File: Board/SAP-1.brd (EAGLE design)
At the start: 100 x 100 mm, 113 parts

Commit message: added RAM module and MAR
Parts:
- added MEMORY_ADDRESS_REGISTER:C1, MEMORY_ADDRESS_REGISTER:C2, RAM:C1, RAM:C10, RAM:C2, RAM:C3, RAM:C4, RAM:C5, RAM:C6, RAM:C7, RAM:C8, RAM:C9: 100n, rcl:C050-024X044
- added MEMORY_ADDRESS_REGISTER:IC1: 74LS173N, 74xx-us:DIL16
- added MEMORY_ADDRESS_REGISTER:IC2, RAM:IC6, RAM:IC7, RAM:IC8: 74LS157N, 74xx-us:DIL16
- added MEMORY_ADDRESS_REGISTER:LED1, MEMORY_ADDRESS_REGISTER:LED2, MEMORY_ADDRESS_REGISTER:LED3, MEMORY_ADDRESS_REGISTER:LED4, RAM:LED1, RAM:LED2, RAM:LED3, RAM:LED4: BLUE, led:LED3MM
- added MEMORY_ADDRESS_REGISTER:PROG: RED, led:LED3MM
- added MEMORY_ADDRESS_REGISTER:R1, MEMORY_ADDRESS_REGISTER:R10, MEMORY_ADDRESS_REGISTER:R2, MEMORY_ADDRESS_REGISTER:R3, MEMORY_ADDRESS_REGISTER:R4, MEMORY_ADDRESS_REGISTER:R9, RAM:R1, RAM:R2, RAM:R3, RAM:R4, RAM:R5, RAM:R6, RAM:R7, RAM:R8: 220, rcl:0204/7
- added MEMORY_ADDRESS_REGISTER:RUN: GREEN, led:LED3MM
- added MEMORY_ADDRESS_REGISTER:S1: Memory Address, switch-dil:DIP04YL
- added MEMORY_ADDRESS_REGISTER:S3: (no value), SparkFun-Switches:SWITCH_SPDT_PTH_11.6X4.0MM_KIT
- added RAM:IC1, RAM:IC2: 74LS189LSN, SAP-1:DIL16
- added RAM:IC3: 74LS245N, 74xx-us:DIL20
- added RAM:IC4, RAM:IC5: 74LS04N, 74xx-us:DIL14
- added RAM:IC9: 74ALS00N, 74xx-us:DIL14
- added RAM:LED5, RAM:LED6, RAM:LED7, RAM:LED8: YELLOW, led:LED3MM
- added RAM:R9: 1k, rcl:0204/7
- added RAM:S1: Write, SparkFun-Switches:TACTILE_SWITCH_PTH_12MM
- added RAM:S2: Memory Data, switch-dil:DIP08YL
- renumbered ALU1:IC1 to ALU:IC1, ALU1:IC2 to ALU:IC2, ALU1:IC3 to ALU:IC3, ALU1:IC4 to ALU:IC4, ALU1:IC5 to ALU:IC5, ALU1:LED1 to ALU:LED1, ALU1:LED2 to ALU:LED2, ALU1:LED3 to ALU:LED3, ALU1:LED4 to ALU:LED4, ALU1:LED5 to ALU:LED5, ALU1:LED6 to ALU:LED6, ALU1:LED7 to ALU:LED7, ALU1:LED8 to ALU:LED8, ALU1:R1 to ALU:R1, ALU1:R2 to ALU:R2, ALU1:R3 to ALU:R3, ALU1:R4 to ALU:R4, ALU1:R5 to ALU:R5, ALU1:R6 to ALU:R6, ALU1:R7 to ALU:R7, ALU1:R8 to ALU:R8
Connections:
- net ALU1:!ENABLE renamed !E0
- net ALU1:CARRY renamed CY
- net ALU1:GND renamed ALU:GND
- net ALU1:N$1 renamed ALU:N$1
- net ALU1:N$18 renamed ALU:N$18
- net ALU1:N$19 renamed ALU:N$19
- net ALU1:N$2 renamed ALU:N$2
- net ALU1:N$20 renamed ALU:N$20
- net ALU1:N$21 renamed ALU:N$21
- net ALU1:N$22 renamed ALU:N$22
- net ALU1:N$23 renamed ALU:N$23
- net ALU1:N$24 renamed ALU:N$24
- net ALU1:N$25 renamed ALU:N$25
- net ALU1:N$3 renamed ALU:N$3
- net ALU1:N$4 renamed ALU:N$4
- net ALU1:N$5 renamed ALU:N$5
- net ALU1:N$6 renamed ALU:N$6
- net ALU1:N$7 renamed ALU:N$7
- net ALU1:N$8 renamed ALU:N$8
- net ALU1:N$9 renamed ALU:N$9
- net ALU1:S1 renamed ALU:S1
- net ALU1:S2 renamed ALU:S2
- net ALU1:S3 renamed ALU:S3
- net ALU1:S4 renamed ALU:S4
- net ALU1:S5 renamed ALU:S5
- net ALU1:S6 renamed ALU:S6
- net ALU1:S7 renamed ALU:S7
- net ALU1:S8 renamed ALU:S8
- net ALU1:SU renamed SU
- net ALU1:VCC renamed ALU:VCC
- net CLK:CLK_HLT renamed HLT
- net IR:!ENABLE renamed !IO
- net IR:!LOAD renamed !II
- net RA:!ENABLE renamed !AO
- net RA:!LOAD renamed !AI
- net RB:!ENABLE renamed !BO
- net RB:!LOAD renamed !BI
- new net !MI: MEMORY_ADDRESS_REGISTER:IC1.10, MEMORY_ADDRESS_REGISTER:IC1.9
- new net !RO: RAM:IC3.19
- new net MEMORY_ADDRESS_REGISTER:CLK_IN: MEMORY_ADDRESS_REGISTER:IC1.7
- new net MEMORY_ADDRESS_REGISTER:CLR: MEMORY_ADDRESS_REGISTER:IC1.15
- new net MEMORY_ADDRESS_REGISTER:GND: MEMORY_ADDRESS_REGISTER:C1.2, MEMORY_ADDRESS_REGISTER:C2.2, MEMORY_ADDRESS_REGISTER:IC1.1, MEMORY_ADDRESS_REGISTER:IC1.2, MEMORY_ADDRESS_REGISTER:IC1.8, MEMORY_ADDRESS_REGISTER:IC2.15, MEMORY_ADDRESS_REGISTER:IC2.8, MEMORY_ADDRESS_REGISTER:R1.2, MEMORY_ADDRESS_REGISTER:R2.2, MEMORY_ADDRESS_REGISTER:R3.2, MEMORY_ADDRESS_REGISTER:R4.2, MEMORY_ADDRESS_REGISTER:S1.1, MEMORY_ADDRESS_REGISTER:S1.2, MEMORY_ADDRESS_REGISTER:S1.3, MEMORY_ADDRESS_REGISTER:S1.4, MEMORY_ADDRESS_REGISTER:S3.2
- new net MEMORY_ADDRESS_REGISTER:I5: MEMORY_ADDRESS_REGISTER:IC1.3, MEMORY_ADDRESS_REGISTER:IC2.3
- new net MEMORY_ADDRESS_REGISTER:I6: MEMORY_ADDRESS_REGISTER:IC1.4, MEMORY_ADDRESS_REGISTER:IC2.6
- new net MEMORY_ADDRESS_REGISTER:I7: MEMORY_ADDRESS_REGISTER:IC1.5, MEMORY_ADDRESS_REGISTER:IC2.10
- new net MEMORY_ADDRESS_REGISTER:I8: MEMORY_ADDRESS_REGISTER:IC1.6, MEMORY_ADDRESS_REGISTER:IC2.13
- new net MEMORY_ADDRESS_REGISTER:N$1: MEMORY_ADDRESS_REGISTER:IC2.2, MEMORY_ADDRESS_REGISTER:S1.8
- new net MEMORY_ADDRESS_REGISTER:N$10: MEMORY_ADDRESS_REGISTER:LED2.K, MEMORY_ADDRESS_REGISTER:R2.1
- new net MEMORY_ADDRESS_REGISTER:N$11: MEMORY_ADDRESS_REGISTER:LED3.K, MEMORY_ADDRESS_REGISTER:R3.1
- new net MEMORY_ADDRESS_REGISTER:N$12: MEMORY_ADDRESS_REGISTER:LED4.K, MEMORY_ADDRESS_REGISTER:R4.1
- new net MEMORY_ADDRESS_REGISTER:N$13: MEMORY_ADDRESS_REGISTER:R10.1, MEMORY_ADDRESS_REGISTER:RUN.K
- new net MEMORY_ADDRESS_REGISTER:N$3: MEMORY_ADDRESS_REGISTER:IC2.5, MEMORY_ADDRESS_REGISTER:S1.7
- new net MEMORY_ADDRESS_REGISTER:N$4: MEMORY_ADDRESS_REGISTER:LED1.K, MEMORY_ADDRESS_REGISTER:R1.1
- new net MEMORY_ADDRESS_REGISTER:N$5: MEMORY_ADDRESS_REGISTER:IC2.11, MEMORY_ADDRESS_REGISTER:S1.6
- new net MEMORY_ADDRESS_REGISTER:N$6: MEMORY_ADDRESS_REGISTER:IC2.14, MEMORY_ADDRESS_REGISTER:S1.5
- new net MEMORY_ADDRESS_REGISTER:N$7: MEMORY_ADDRESS_REGISTER:R10.2, MEMORY_ADDRESS_REGISTER:S3.3
- new net MEMORY_ADDRESS_REGISTER:N$9: MEMORY_ADDRESS_REGISTER:PROG.K, MEMORY_ADDRESS_REGISTER:R9.1
- new net MEMORY_ADDRESS_REGISTER:VCC: MEMORY_ADDRESS_REGISTER:C1.1, MEMORY_ADDRESS_REGISTER:C2.1, MEMORY_ADDRESS_REGISTER:IC1.16, MEMORY_ADDRESS_REGISTER:IC2.16, MEMORY_ADDRESS_REGISTER:PROG.A, MEMORY_ADDRESS_REGISTER:RUN.A
- new net N$17: MEMORY_ADDRESS_REGISTER:IC2.4, MEMORY_ADDRESS_REGISTER:LED1.A, RAM:IC1.1, RAM:IC2.1
- new net N$18: MEMORY_ADDRESS_REGISTER:IC2.7, MEMORY_ADDRESS_REGISTER:LED2.A, RAM:IC1.15, RAM:IC2.15
- new net N$19: MEMORY_ADDRESS_REGISTER:IC2.9, MEMORY_ADDRESS_REGISTER:LED3.A, RAM:IC1.14, RAM:IC2.14
- new net N$20: MEMORY_ADDRESS_REGISTER:IC2.12, MEMORY_ADDRESS_REGISTER:LED4.A, RAM:IC1.13, RAM:IC2.13
- new net N$21: MEMORY_ADDRESS_REGISTER:IC2.1, MEMORY_ADDRESS_REGISTER:R9.2, MEMORY_ADDRESS_REGISTER:S3.1, RAM:IC6.1, RAM:IC7.1, RAM:IC8.1
- new net RAM:!WRITE: RAM:IC1.3, RAM:IC2.3, RAM:IC8.4
- new net RAM:B1: RAM:IC1.4, RAM:IC6.4
- new net RAM:B2: RAM:IC1.6, RAM:IC6.7
- new net RAM:B3: RAM:IC1.10, RAM:IC6.9
- new net RAM:B4: RAM:IC1.12, RAM:IC6.12
- new net RAM:B5: RAM:IC2.4, RAM:IC7.4
- new net RAM:B6: RAM:IC2.6, RAM:IC7.7
- new net RAM:B7: RAM:IC2.10, RAM:IC7.9
- new net RAM:B8: RAM:IC2.12, RAM:IC7.12
- new net RAM:CLK_IN: RAM:C10.1
- new net RAM:GND: RAM:C1.2, RAM:C2.2, RAM:C3.2, RAM:C4.2, RAM:C5.2, RAM:C6.2, RAM:C7.2, RAM:C8.2, RAM:C9.2, RAM:IC1.2, RAM:IC1.8, RAM:IC2.2, RAM:IC2.8, RAM:IC3.10, RAM:IC4.7, RAM:IC5.7, RAM:IC6.15, RAM:IC6.8, RAM:IC7.15, RAM:IC7.8, RAM:IC8.15, RAM:IC8.8, RAM:IC9.7, RAM:R1.2, RAM:R2.2, RAM:R3.2, RAM:R4.2, RAM:R5.2, RAM:R6.2, RAM:R7.2, RAM:R8.2, RAM:R9.1, RAM:S1.1, RAM:S2.1, RAM:S2.2, RAM:S2.3, RAM:S2.4, RAM:S2.5, RAM:S2.6, RAM:S2.7, RAM:S2.8
- new net RAM:I1: RAM:IC3.2, RAM:IC4.2, RAM:LED1.A
- new net RAM:I2: RAM:IC3.3, RAM:IC4.4, RAM:LED2.A
- new net RAM:I3: RAM:IC3.4, RAM:IC4.6, RAM:LED3.A
- new net RAM:I4: RAM:IC3.5, RAM:IC4.8, RAM:LED4.A
- new net RAM:I5: RAM:IC3.6, RAM:IC5.2, RAM:LED5.A
- new net RAM:I6: RAM:IC3.7, RAM:IC5.4, RAM:LED6.A
- new net RAM:I7: RAM:IC3.8, RAM:IC5.6, RAM:LED7.A
- new net RAM:I8: RAM:IC3.9, RAM:IC5.8, RAM:LED8.A
- new net RAM:N$1: RAM:IC1.5, RAM:IC4.1
- new net RAM:N$10: RAM:LED2.K, RAM:R2.1
- new net RAM:N$11: RAM:LED3.K, RAM:R3.1
- new net RAM:N$12: RAM:LED4.K, RAM:R4.1
- new net RAM:N$13: RAM:LED5.K, RAM:R5.1
- new net RAM:N$14: RAM:LED6.K, RAM:R6.1
- new net RAM:N$15: RAM:LED7.K, RAM:R7.1
- new net RAM:N$16: RAM:LED8.K, RAM:R8.1
- new net RAM:N$17: RAM:IC8.2, RAM:S1.3
- new net RAM:N$18: RAM:IC7.14, RAM:S2.9
- new net RAM:N$19: RAM:IC7.11, RAM:S2.10
- new net RAM:N$2: RAM:IC1.7, RAM:IC4.3
- new net RAM:N$20: RAM:IC7.5, RAM:S2.11
- new net RAM:N$21: RAM:IC7.2, RAM:S2.12
- new net RAM:N$22: RAM:IC6.14, RAM:S2.13
- new net RAM:N$23: RAM:IC6.11, RAM:S2.14
- new net RAM:N$24: RAM:IC6.5, RAM:S2.15
- new net RAM:N$25: RAM:IC6.2, RAM:S2.16
- new net RAM:N$26: RAM:IC8.3, RAM:IC9.3
- new net RAM:N$27: RAM:C10.2, RAM:IC9.2, RAM:R9.2
- new net RAM:N$3: RAM:IC1.9, RAM:IC4.5
- new net RAM:N$4: RAM:IC1.11, RAM:IC4.9
- new net RAM:N$5: RAM:IC2.5, RAM:IC5.1
- new net RAM:N$6: RAM:IC2.7, RAM:IC5.3
- new net RAM:N$7: RAM:IC2.9, RAM:IC5.5
- new net RAM:N$8: RAM:IC2.11, RAM:IC5.9
- new net RAM:N$9: RAM:LED1.K, RAM:R1.1
- new net RAM:VCC: RAM:C1.1, RAM:C2.1, RAM:C3.1, RAM:C4.1, RAM:C5.1, RAM:C6.1, RAM:C7.1, RAM:C8.1, RAM:C9.1, RAM:IC1.16, RAM:IC2.16, RAM:IC3.1, RAM:IC3.20, RAM:IC4.14, RAM:IC5.14, RAM:IC6.16, RAM:IC7.16, RAM:IC8.16, RAM:IC9.14
- new net RI: RAM:IC9.1
- net D1: now also MEMORY_ADDRESS_REGISTER:IC1.14, RAM:IC3.18, RAM:IC6.3
- net D2: now also MEMORY_ADDRESS_REGISTER:IC1.13, RAM:IC3.17, RAM:IC6.6
- net D3: now also MEMORY_ADDRESS_REGISTER:IC1.12, RAM:IC3.16, RAM:IC6.10
- net D4: now also MEMORY_ADDRESS_REGISTER:IC1.11, RAM:IC3.15, RAM:IC6.13
- net D5: now also RAM:IC3.14, RAM:IC7.3
- net D6: now also RAM:IC3.13, RAM:IC7.6
- net D7: now also RAM:IC3.12, RAM:IC7.10
- net D8: now also RAM:IC3.11, RAM:IC7.13
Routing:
- net D8: track 66.1 -> 0.00 mm
- net D7: track 63.5 -> 0.00 mm
- net D6: track 62.6 -> 0.00 mm
- net D5: track 60.6 -> 0.00 mm
- net D4: track 60.1 -> 0.00 mm
- net D3: track 54.5 -> 0.00 mm
- net D2: track 49.7 -> 0.00 mm
- net D1: track 45.6 -> 0.00 mm

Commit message: added program counter
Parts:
- added PC:C1, PC:C2: 100n, rcl:C050-024X044
- added PC:IC1: 74LS161N, 74xx-us:DIL16
- added PC:IC2: 74LS245N, 74xx-us:DIL20
- added PC:LED1, PC:LED2, PC:LED3, PC:LED4: BLUE, led:LED3MM
- added PC:R1, PC:R2, PC:R3, PC:R4: 220, rcl:0204/7
- renumbered MEMORY_ADDRESS_REGISTER:C1 to MAR:C1, MEMORY_ADDRESS_REGISTER:C2 to MAR:C2, MEMORY_ADDRESS_REGISTER:IC1 to MAR:IC1, MEMORY_ADDRESS_REGISTER:IC2 to MAR:IC2, MEMORY_ADDRESS_REGISTER:LED1 to MAR:LED1, MEMORY_ADDRESS_REGISTER:LED2 to MAR:LED2, MEMORY_ADDRESS_REGISTER:LED3 to MAR:LED3, MEMORY_ADDRESS_REGISTER:LED4 to MAR:LED4, MEMORY_ADDRESS_REGISTER:PROG to MAR:PROG, MEMORY_ADDRESS_REGISTER:R1 to MAR:R1, MEMORY_ADDRESS_REGISTER:R10 to MAR:R10, MEMORY_ADDRESS_REGISTER:R2 to MAR:R2, MEMORY_ADDRESS_REGISTER:R3 to MAR:R3, MEMORY_ADDRESS_REGISTER:R4 to MAR:R4, MEMORY_ADDRESS_REGISTER:R9 to MAR:R9, MEMORY_ADDRESS_REGISTER:RUN to MAR:RUN, MEMORY_ADDRESS_REGISTER:S1 to MAR:S1, MEMORY_ADDRESS_REGISTER:S3 to MAR:S3
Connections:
- net MEMORY_ADDRESS_REGISTER:CLK_IN renamed MAR:CLK_IN
- net MEMORY_ADDRESS_REGISTER:CLR renamed MAR:CLR
- net MEMORY_ADDRESS_REGISTER:GND renamed MAR:GND
- net MEMORY_ADDRESS_REGISTER:I5 renamed MAR:I5
- net MEMORY_ADDRESS_REGISTER:I6 renamed MAR:I6
- net MEMORY_ADDRESS_REGISTER:I7 renamed MAR:I7
- net MEMORY_ADDRESS_REGISTER:I8 renamed MAR:I8
- net MEMORY_ADDRESS_REGISTER:N$1 renamed MAR:N$1
- net MEMORY_ADDRESS_REGISTER:N$10 renamed MAR:N$10
- net MEMORY_ADDRESS_REGISTER:N$11 renamed MAR:N$11
- net MEMORY_ADDRESS_REGISTER:N$12 renamed MAR:N$12
- net MEMORY_ADDRESS_REGISTER:N$13 renamed MAR:N$13
- net MEMORY_ADDRESS_REGISTER:N$3 renamed MAR:N$3
- net MEMORY_ADDRESS_REGISTER:N$4 renamed MAR:N$4
- net MEMORY_ADDRESS_REGISTER:N$5 renamed MAR:N$5
- net MEMORY_ADDRESS_REGISTER:N$6 renamed MAR:N$6
- net MEMORY_ADDRESS_REGISTER:N$7 renamed MAR:N$7
- net MEMORY_ADDRESS_REGISTER:N$9 renamed MAR:N$9
- net MEMORY_ADDRESS_REGISTER:VCC renamed MAR:VCC
- new net !CO: PC:IC2.19
- new net !JP: PC:IC1.9
- new net CE: PC:IC1.10, PC:IC1.7
- new net PC:!CLR: PC:IC1.1
- new net PC:CLK_IN: PC:IC1.2
- new net PC:GND: PC:C1.2, PC:C2.2, PC:IC1.8, PC:IC2.10, PC:IC2.6, PC:IC2.7, PC:IC2.8, PC:IC2.9, PC:R1.2, PC:R2.2, PC:R3.2, PC:R4.2
- new net PC:N$10: PC:LED2.K, PC:R2.1
- new net PC:N$11: PC:LED3.K, PC:R3.1
- new net PC:N$12: PC:LED4.K, PC:R4.1
- new net PC:N$4: PC:LED1.K, PC:R1.1
- new net PC:Q1: PC:IC1.14, PC:IC2.2, PC:LED1.A
- new net PC:Q2: PC:IC1.13, PC:IC2.3, PC:LED2.A
- new net PC:Q3: PC:IC1.12, PC:IC2.4, PC:LED3.A
- new net PC:Q4: PC:IC1.11, PC:IC2.5, PC:LED4.A
- new net PC:VCC: PC:C1.1, PC:C2.1, PC:IC1.16, PC:IC2.1, PC:IC2.20
- net D1: now also PC:IC1.3, PC:IC2.18
- net D2: now also PC:IC1.4, PC:IC2.17
- net D3: now also PC:IC1.5, PC:IC2.16
- net D4: now also PC:IC1.6, PC:IC2.15

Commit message: added output module
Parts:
- added OUT:C1, OUT:C2, OUT:C3, OUT:C4, OUT:C5, OUT:C6, OUT:C8: 100n, rcl:C050-024X044
- added OUT:C7: 10n, rcl:C050-024X044
- added OUT:D1, OUT:D2, OUT:D3, OUT:D4: (no value), special:7SEG-13
- added OUT:IC1: 28C16AP, microchip:DIL24-6
- added OUT:IC2: 74ALS08N, 74xx-us:DIL14
- added OUT:IC3: 74273N, 74xx-us:DIL20
- added OUT:IC4: LM555, SAP-1:DIP8
- added OUT:IC5: 74LS76N, 74xx-us:DIL16
- added OUT:IC6: 74LS139N, 74xx-us:DIL16
- added OUT:R1: 1k, rcl:0204/7
- added OUT:R3: 100k, rcl:0204/7
- added OUT:S3: 2's Complement, SparkFun-Switches:SWITCH_SPDT_PTH_11.6X4.0MM_KIT
- RAM:C10: value 100n -> 10n
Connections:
- new net OUT:!CLR: OUT:IC3.1
- new net OUT:2SC: OUT:IC1.19, OUT:S3.2
- new net OUT:CLK_IN: OUT:IC2.1
- new net OUT:DIG1: OUT:D1.3, OUT:D1.8, OUT:IC6.4
- new net OUT:DIG2: OUT:D2.3, OUT:D2.8, OUT:IC6.5
- new net OUT:DIG3: OUT:D3.3, OUT:D3.8, OUT:IC6.6
- new net OUT:DIG4: OUT:D4.3, OUT:D4.8, OUT:IC6.7
- new net OUT:DISP_CLK: OUT:IC4.3, OUT:IC5.1
- new net OUT:DS1: OUT:IC1.23, OUT:IC5.14, OUT:IC5.6, OUT:IC6.2
- new net OUT:DS2: OUT:IC1.22, OUT:IC5.10, OUT:IC6.3
- new net OUT:GND: OUT:C1.2, OUT:C2.2, OUT:C3.2, OUT:C4.2, OUT:C5.2, OUT:C6.2, OUT:C7.2, OUT:C8.2, OUT:IC1.12, OUT:IC1.18, OUT:IC1.20, OUT:IC2.7, OUT:IC3.10, OUT:IC4.1, OUT:IC5.13, OUT:IC6.1, OUT:IC6.8, OUT:S3.1
- new net OUT:LOAD: OUT:IC2.2
- new net OUT:N$1: OUT:IC1.8, OUT:IC3.2
- new net OUT:N$13: OUT:IC4.7, OUT:R1.1, OUT:R3.2
- new net OUT:N$15: OUT:C8.1, OUT:IC4.5
- new net OUT:N$16: OUT:C7.1, OUT:IC4.2, OUT:IC4.6, OUT:R3.1
- new net OUT:N$2: OUT:IC1.7, OUT:IC3.5
- new net OUT:N$3: OUT:IC1.6, OUT:IC3.6
- new net OUT:N$4: OUT:IC1.5, OUT:IC3.9
- new net OUT:N$5: OUT:IC1.4, OUT:IC3.12
- new net OUT:N$6: OUT:IC1.3, OUT:IC3.15
- new net OUT:N$7: OUT:IC1.2, OUT:IC3.16
- new net OUT:N$8: OUT:IC1.1, OUT:IC3.19
- new net OUT:N$9: OUT:IC2.3, OUT:IC3.11
- new net OUT:SEG_A: OUT:D1.7, OUT:D2.7, OUT:D3.7, OUT:D4.7, OUT:IC1.9
- new net OUT:SEG_B: OUT:D1.6, OUT:D2.6, OUT:D3.6, OUT:D4.6, OUT:IC1.10
- new net OUT:SEG_C: OUT:D1.4, OUT:D2.4, OUT:D3.4, OUT:D4.4, OUT:IC1.11
- new net OUT:SEG_D: OUT:D1.2, OUT:D2.2, OUT:D3.2, OUT:D4.2, OUT:IC1.13
- new net OUT:SEG_DP: OUT:D1.5, OUT:D2.5, OUT:D3.5, OUT:D4.5, OUT:IC1.17
- new net OUT:SEG_E: OUT:D1.1, OUT:D2.1, OUT:D3.1, OUT:D4.1, OUT:IC1.14
- new net OUT:SEG_F: OUT:D1.9, OUT:D2.9, OUT:D3.9, OUT:D4.9, OUT:IC1.15
- new net OUT:SEG_G: OUT:D1.10, OUT:D2.10, OUT:D3.10, OUT:D4.10, OUT:IC1.16
- new net OUT:VCC: OUT:C1.1, OUT:C2.1, OUT:C3.1, OUT:C4.1, OUT:C5.1, OUT:C6.1, OUT:IC1.21, OUT:IC1.24, OUT:IC2.14, OUT:IC3.20, OUT:IC4.4, OUT:IC4.8, OUT:IC5.12, OUT:IC5.16, OUT:IC5.2, OUT:IC5.3, OUT:IC5.4, OUT:IC5.5, OUT:IC5.7, OUT:IC5.8, OUT:IC5.9, OUT:IC6.16, OUT:R1.2, OUT:S3.3
- net D1: now also OUT:IC3.3
- net D2: now also OUT:IC3.4
- net D3: now also OUT:IC3.7
- net D4: now also OUT:IC3.8
- net D5: now also OUT:IC3.13
- net D6: now also OUT:IC3.14
- net D7: now also OUT:IC3.17
- net D8: now also OUT:IC3.18

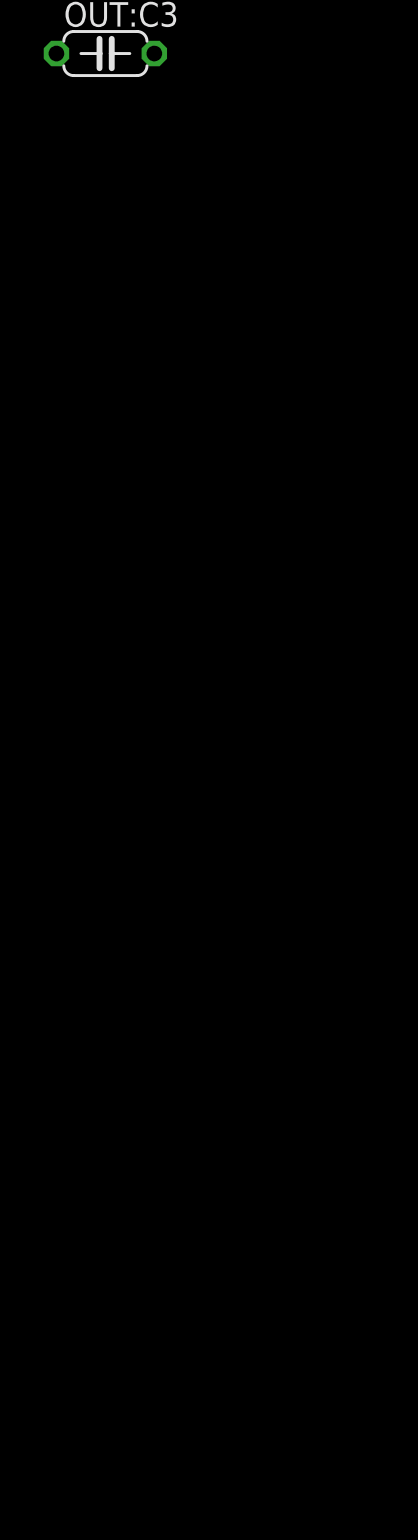
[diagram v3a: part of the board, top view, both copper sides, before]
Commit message: connected seperate modules
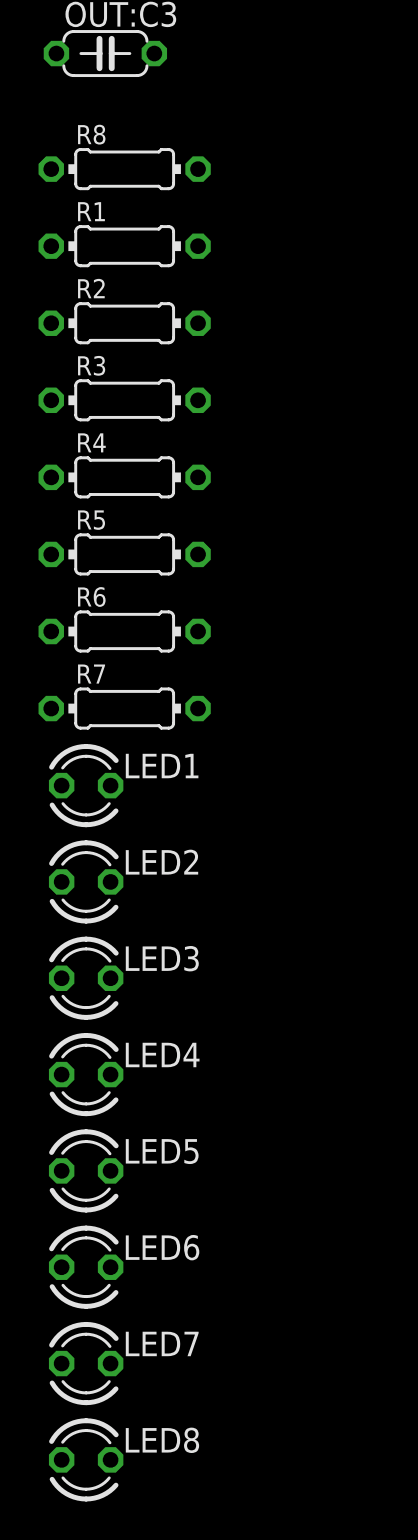
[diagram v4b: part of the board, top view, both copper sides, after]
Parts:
- added LED1, LED2, LED3, LED4, LED5, LED6, LED7, LED8: (no value), led:LED3MM
- added R1, R2, R3, R4, R5, R6, R7, R8: 10k, rcl:0204/7
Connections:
- net OUT:LOAD renamed OI
- removed net CLK:CLK_OUT: CLK:IC6.8, CLK:LED1.A
- removed net IR:CLK_IN: IR:IC2.7, IR:IC3.7
- removed net MAR:CLK_IN: MAR:IC1.7
- removed net OUT:CLK_IN: OUT:IC2.1
- removed net PC:CLK_IN: PC:IC1.2
- removed net RA:CLK_IN: RA:IC2.7, RA:IC3.7
- removed net RAM:CLK_IN: RAM:C10.1
- removed net RB:CLK_IN: RB:IC2.7, RB:IC3.7
- new net GND: LED1.K, LED2.K, LED3.K, LED4.K, LED5.K, LED6.K, LED7.K, LED8.K, R1.1, R2.1, R3.1, R4.1, R5.1, R6.1, R7.1, R8.1
- new net N$22: CLK:IC6.8, CLK:LED1.A, IR:IC2.7, IR:IC3.7, MAR:IC1.7, OUT:IC2.1, PC:IC1.2, RA:IC2.7, RA:IC3.7, RAM:C10.1, RB:IC2.7, RB:IC3.7
- net D1: now also LED1.A, R1.2
- net D2: now also LED2.A, R2.2
- net D3: now also LED3.A, R3.2
- net D4: now also LED4.A, R4.2
- net D5: now also LED5.A, R5.2
- net D6: now also LED6.A, R6.2
- net D7: now also LED7.A, R7.2
- net D8: now also LED8.A, R8.2
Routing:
- net RA:CLK_IN: track 31.8 -> 0.00 mm
- net N$22: track 0.00 -> 31.8 mm

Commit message: added instruction decoder module
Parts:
- removed ALU:R1, ALU:R2, ALU:R3, ALU:R4, ALU:R5, ALU:R6, ALU:R7, ALU:R8, CLK:R4, IR:R1, IR:R2, IR:R3, IR:R4, IR:R5, IR:R6, IR:R7, IR:R8, MAR:R1, MAR:R2, MAR:R3, MAR:R4, PC:R1, PC:R2, PC:R3, PC:R4, RA:R1, RA:R2, RA:R3, RA:R4, RA:R5, RA:R6, RA:R7, RA:R8, RAM:R1, RAM:R2, RAM:R3, RAM:R4, RAM:R5, RAM:R6, RAM:R7, RAM:R8, RB:R1, RB:R2, RB:R3, RB:R4, RB:R5, RB:R6, RB:R7, RB:R8: 220, rcl:0204/7
- added ID:C1, ID:C2, ID:C3, ID:C4, ID:C5, ID:C6: 100n, rcl:C050-024X044
- added ID:IC1, ID:IC2: 28C16AP, microchip:DIL24-6
- added ID:IC3, ID:IC4: 74ALS04N, 74xx-us:DIL14
- added ID:IC5: 74LS161N, 74xx-us:DIL16
- added ID:IC6: 74LS138N, 74xx-us:DIL16
- added ID:IC7: 74ALS00N, 74xx-us:DIL14
- added ID:LED1, ID:LED10, ID:LED11, ID:LED12, ID:LED13, ID:LED14, ID:LED15, ID:LED16, ID:LED17, ID:LED18, ID:LED19, ID:LED2, ID:LED20, ID:LED3, ID:LED4, ID:LED5, ID:LED6, ID:LED7, ID:LED8, ID:LED9: (no value), led:LED3MM
- added ID:R1, ID:R10, ID:R11, ID:R12, ID:R13, ID:R14, ID:R15, ID:R2, ID:R3, ID:R4, ID:R5, ID:R6, ID:R7, ID:R8, ID:R9: 220, rcl:0204/7
- added ID:R16: 10k, rcl:0204/7
- added ID:S1: Reset, SparkFun-Switches:TACTILE_SWITCH_PTH_12MM
- added R10, R11, R12, R13, R14, R15, R16, R9: 470, rcl:0204/7
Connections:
- net IR:I1 renamed IR:B1
- net IR:I2 renamed IR:B2
- net IR:I3 renamed IR:B3
- net IR:I4 renamed IR:B4
- net IR:I5 renamed IR:B5
- net IR:I6 renamed IR:B6
- net IR:I7 renamed IR:B7
- net IR:I8 renamed IR:B8
- removed net !E0: ALU:IC5.19
- removed net ALU:N$2: ALU:LED2.K, ALU:R2.1
- removed net ALU:N$3: ALU:LED3.K, ALU:R3.1
- removed net ALU:N$4: ALU:LED4.K, ALU:R4.1
- removed net ALU:N$5: ALU:LED5.K, ALU:R5.1
- removed net ALU:N$6: ALU:LED6.K, ALU:R6.1
- removed net ALU:N$7: ALU:LED7.K, ALU:R7.1
- removed net ALU:N$8: ALU:LED8.K, ALU:R8.1
- removed net CLK:N$4: CLK:LED1.K, CLK:R4.2
- removed net IR:CLR: IR:IC2.15, IR:IC3.15
- removed net IR:N$10: IR:LED2.K, IR:R2.1
- removed net IR:N$11: IR:LED3.K, IR:R3.1
- removed net IR:N$12: IR:LED4.K, IR:R4.1
- removed net IR:N$13: IR:LED5.K, IR:R5.1
- removed net IR:N$14: IR:LED6.K, IR:R6.1
- removed net IR:N$15: IR:LED7.K, IR:R7.1
- removed net IR:N$16: IR:LED8.K, IR:R8.1
- removed net MAR:CLR: MAR:IC1.15
- removed net MAR:N$10: MAR:LED2.K, MAR:R2.1
- removed net MAR:N$11: MAR:LED3.K, MAR:R3.1
- removed net MAR:N$12: MAR:LED4.K, MAR:R4.1
- removed net MAR:N$4: MAR:LED1.K, MAR:R1.1
- removed net OUT:!CLR: OUT:IC3.1
- removed net PC:!CLR: PC:IC1.1
- removed net PC:N$10: PC:LED2.K, PC:R2.1
- removed net PC:N$11: PC:LED3.K, PC:R3.1
- removed net PC:N$12: PC:LED4.K, PC:R4.1
- removed net PC:N$4: PC:LED1.K, PC:R1.1
- removed net RA:CLR: RA:IC2.15, RA:IC3.15
- removed net RA:N$10: RA:LED2.K, RA:R2.1
- removed net RA:N$11: RA:LED3.K, RA:R3.1
- removed net RA:N$12: RA:LED4.K, RA:R4.1
- removed net RA:N$13: RA:LED5.K, RA:R5.1
- removed net RA:N$14: RA:LED6.K, RA:R6.1
- removed net RA:N$15: RA:LED7.K, RA:R7.1
- removed net RA:N$16: RA:LED8.K, RA:R8.1
- removed net RAM:N$10: RAM:LED2.K, RAM:R2.1
- removed net RAM:N$11: RAM:LED3.K, RAM:R3.1
- removed net RAM:N$12: RAM:LED4.K, RAM:R4.1
- removed net RAM:N$13: RAM:LED5.K, RAM:R5.1
- removed net RAM:N$14: RAM:LED6.K, RAM:R6.1
- removed net RAM:N$15: RAM:LED7.K, RAM:R7.1
- removed net RAM:N$16: RAM:LED8.K, RAM:R8.1
- removed net RAM:N$9: RAM:LED1.K, RAM:R1.1
- removed net RB:CLR: RB:IC2.15, RB:IC3.15
- removed net RB:N$10: RB:LED2.K, RB:R2.1
- removed net RB:N$11: RB:LED3.K, RB:R3.1
- removed net RB:N$12: RB:LED4.K, RB:R4.1
- removed net RB:N$13: RB:LED5.K, RB:R5.1
- removed net RB:N$14: RB:LED6.K, RB:R6.1
- removed net RB:N$15: RB:LED7.K, RB:R7.1
- removed net RB:N$4: RB:LED1.K, RB:R1.1
- new net !CLR: ID:IC7.10, ID:IC7.3, ID:IC7.4, ID:IC7.5, OUT:IC3.1, PC:IC1.1
- new net !EO: ALU:IC5.19, ID:IC4.2, ID:LED9.A
- new net CLR: ID:IC7.6, IR:IC2.15, IR:IC3.15, MAR:IC1.15, RA:IC2.15, RA:IC3.15, RB:IC2.15, RB:IC3.15
- new net ID:!T0: ID:IC6.15, ID:LED16.A
- new net ID:!T1: ID:IC6.14, ID:LED17.A
- new net ID:!T2: ID:IC6.13, ID:LED18.A
- new net ID:!T3: ID:IC6.12, ID:LED19.A
- new net ID:!T4: ID:IC6.11, ID:LED20.A
- new net ID:GND: ID:C1.2, ID:C2.2, ID:C3.2, ID:C4.2, ID:C5.2, ID:C6.2, ID:IC1.1, ID:IC1.12, ID:IC1.18, ID:IC1.19, ID:IC1.20, ID:IC1.22, ID:IC1.23, ID:IC2.1, ID:IC2.12, ID:IC2.18, ID:IC2.19, ID:IC2.20, ID:IC2.22, ID:IC2.23, ID:IC3.7, ID:IC4.7, ID:IC5.8, ID:IC6.4, ID:IC6.5, ID:IC6.8, ID:IC7.7, ID:LED16.K, ID:LED17.K, ID:LED18.K, ID:LED19.K, ID:LED20.K, ID:R1.1, ID:R10.1, ID:R11.1, ID:R12.1, ID:R13.1, ID:R14.1, ID:R15.1, ID:R16.1, ID:R2.1, ID:R3.1, ID:R4.1, ID:R5.1, ID:R6.1, ID:R7.1, ID:R8.1, ID:R9.1
- new net ID:MI1: ID:IC1.8, ID:IC2.8, ID:IC5.14, ID:IC6.1
- new net ID:MI2: ID:IC1.7, ID:IC2.7, ID:IC5.13, ID:IC6.2
- new net ID:MI3: ID:IC1.6, ID:IC2.6, ID:IC5.12, ID:IC6.3
- new net ID:N$1: ID:LED1.K, ID:R1.2
- new net ID:N$10: ID:LED10.K, ID:R10.2
- new net ID:N$11: ID:LED11.K, ID:R11.2
- new net ID:N$12: ID:LED12.K, ID:R12.2
- new net ID:N$13: ID:LED13.K, ID:R13.2
- new net ID:N$14: ID:LED14.K, ID:R14.2
- new net ID:N$15: ID:LED15.K, ID:R15.2
- new net ID:N$16: ID:IC7.1, ID:IC7.2, ID:R16.2, ID:S1.3
- new net ID:N$17: ID:IC5.1, ID:IC7.11
- new net ID:N$18: ID:IC7.12, ID:IC7.13, ID:IC7.8
- new net ID:N$19: ID:IC6.10, ID:IC7.9
- new net ID:N$2: ID:LED2.K, ID:R2.2
- new net ID:N$20: ID:IC1.10, ID:IC3.1
- new net ID:N$21: ID:IC1.11, ID:IC3.3
- new net ID:N$22: ID:IC1.14, ID:IC3.5
- new net ID:N$23: ID:IC1.15, ID:IC3.9
- new net ID:N$24: ID:IC1.16, ID:IC3.11
- new net ID:N$25: ID:IC1.17, ID:IC3.13
- new net ID:N$26: ID:IC2.9, ID:IC4.1
- new net ID:N$27: ID:IC2.11, ID:IC4.3
- new net ID:N$28: ID:IC2.15, ID:IC4.5
- new net ID:N$29: ID:IC2.16, ID:IC4.9
- new net ID:N$3: ID:LED3.K, ID:R3.2
- new net ID:N$4: ID:LED4.K, ID:R4.2
- new net ID:N$5: ID:LED5.K, ID:R5.2
- new net ID:N$6: ID:LED6.K, ID:R6.2
- new net ID:N$7: ID:LED7.K, ID:R7.2
- new net ID:N$8: ID:LED8.K, ID:R8.2
- new net ID:N$9: ID:LED9.K, ID:R9.2
- new net ID:VCC: ID:C1.1, ID:C2.1, ID:C3.1, ID:C4.1, ID:C5.1, ID:C6.1, ID:IC1.21, ID:IC1.24, ID:IC2.21, ID:IC2.24, ID:IC3.14, ID:IC4.14, ID:IC5.10, ID:IC5.16, ID:IC5.7, ID:IC5.9, ID:IC6.16, ID:IC6.6, ID:IC7.14, ID:S1.1
- new net N$23: LED1.A, R9.1
- new net N$24: LED2.A, R10.1
- new net N$25: LED3.A, R11.1
- new net N$26: LED4.A, R12.1
- new net N$27: LED5.A, R13.1
- new net N$28: LED6.A, R14.1
- new net N$29: LED7.A, R15.1
- new net N$30: LED8.A, R16.1
- new net N$31: ID:IC1.5, ID:IC2.5, IR:IC1.14
- new net N$32: CLK:IC7.6, ID:IC5.2
- new net N$33: ID:IC1.4, ID:IC2.4, IR:IC1.13
- new net N$34: ID:IC1.3, ID:IC2.3, IR:IC1.12
- new net N$35: ID:IC1.2, ID:IC2.2, IR:IC1.11
- net !AI: now also ID:IC3.12, ID:LED8.A
- net !AO: now also ID:IC3.10, ID:LED7.A
- net !BI: now also ID:IC4.4, ID:LED11.A
- net !CO: now also ID:IC4.6, ID:LED14.A
- net !II: now also ID:IC3.8, ID:LED6.A
- net !IO: now also ID:IC3.6, ID:LED5.A
- net !JP: now also ID:IC4.8, ID:LED15.A
- net !MI: now also ID:IC3.2, ID:LED2.A
- net !RO: now also ID:IC3.4, ID:LED3.A
- net ALU:GND: no longer ALU:R1.2, ALU:R2.2, ALU:R3.2, ALU:R4.2, ALU:R5.2, ALU:R6.2, ALU:R7.2, ALU:R8.2
- net ALU:N$9: now also ALU:LED2.K, ALU:LED3.K, ALU:LED4.K, ALU:LED5.K, ALU:LED6.K, ALU:LED7.K, ALU:LED8.K; no longer ALU:R1.1
- net CE: now also ID:IC2.14, ID:LED13.A
- net CLK:GND: now also CLK:LED1.K; no longer CLK:R4.1
- net D1: now also R9.2; no longer LED1.A
- net D2: now also R10.2; no longer LED2.A
- net D3: now also R11.2; no longer LED3.A
- net D4: now also R12.2; no longer LED4.A
- net D5: now also R13.2; no longer LED5.A
- net D6: now also R14.2; no longer LED6.A
- net D7: now also R15.2; no longer LED7.A
- net D8: now also R16.2; no longer LED8.A
- net HLT: now also ID:IC1.9, ID:LED1.A
- net IR:D5: no longer IR:IC1.14
- net IR:D6: no longer IR:IC1.13
- net IR:D7: no longer IR:IC1.12
- net IR:D8: no longer IR:IC1.11
- net IR:GND: no longer IR:R1.2, IR:R2.2, IR:R3.2, IR:R4.2, IR:R5.2, IR:R6.2, IR:R7.2, IR:R8.2
- net IR:N$4: now also IR:LED2.K, IR:LED3.K, IR:LED4.K, IR:LED5.K, IR:LED6.K, IR:LED7.K, IR:LED8.K; no longer IR:R1.1
- net MAR:GND: now also MAR:LED1.K, MAR:LED2.K, MAR:LED3.K, MAR:LED4.K; no longer MAR:R1.2, MAR:R2.2, MAR:R3.2, MAR:R4.2
- net N$22: now also CLK:IC7.5
- net OI: now also ID:IC2.13, ID:LED12.A
- net PC:GND: now also PC:LED1.K, PC:LED2.K, PC:LED3.K, PC:LED4.K; no longer PC:R1.2, PC:R2.2, PC:R3.2, PC:R4.2
- net RA:GND: no longer RA:R1.2, RA:R2.2, RA:R3.2, RA:R4.2, RA:R5.2, RA:R6.2, RA:R7.2, RA:R8.2
- net RA:N$4: now also RA:LED2.K, RA:LED3.K, RA:LED4.K, RA:LED5.K, RA:LED6.K, RA:LED7.K, RA:LED8.K; no longer RA:R1.1
- net RAM:GND: now also RAM:LED1.K, RAM:LED2.K, RAM:LED3.K, RAM:LED4.K, RAM:LED5.K, RAM:LED6.K, RAM:LED7.K, RAM:LED8.K; no longer RAM:R1.2, RAM:R2.2, RAM:R3.2, RAM:R4.2, RAM:R5.2, RAM:R6.2, RAM:R7.2, RAM:R8.2
- net RB:GND: no longer RB:R1.2, RB:R2.2, RB:R3.2, RB:R4.2, RB:R5.2, RB:R6.2, RB:R7.2, RB:R8.2
- net RB:N$16: now also RB:LED1.K, RB:LED2.K, RB:LED3.K, RB:LED4.K, RB:LED5.K, RB:LED6.K, RB:LED7.K; no longer RB:R8.1
- net RI: now also ID:IC1.13, ID:LED4.A
- net SU: now also ID:IC2.10, ID:LED10.A
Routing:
- net RA:CLR: track 50.7 -> 0.00 mm
- net CLR: track 0.00 -> 50.7 mm
- net RA:N$4: track 2.54 -> 0.00 mm
- net RA:N$16: track 2.54 -> 0.00 mm
- net RA:N$15: track 2.54 -> 0.00 mm
- net RA:N$14: track 2.54 -> 0.00 mm
- net RA:N$13: track 2.54 -> 0.00 mm
- net RA:N$12: track 2.54 -> 0.00 mm
- net RA:N$11: track 2.54 -> 0.00 mm
- net RA:N$10: track 2.54 -> 0.00 mm
